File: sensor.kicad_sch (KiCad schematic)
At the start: 35 parts, among them J10 Conn_01x01_Pin, J5 Conn_01x07_Pin, J8 Conn_01x08_Pin, U4 mXT336UD-MAU002, U5 MIC5504-3.3YM5

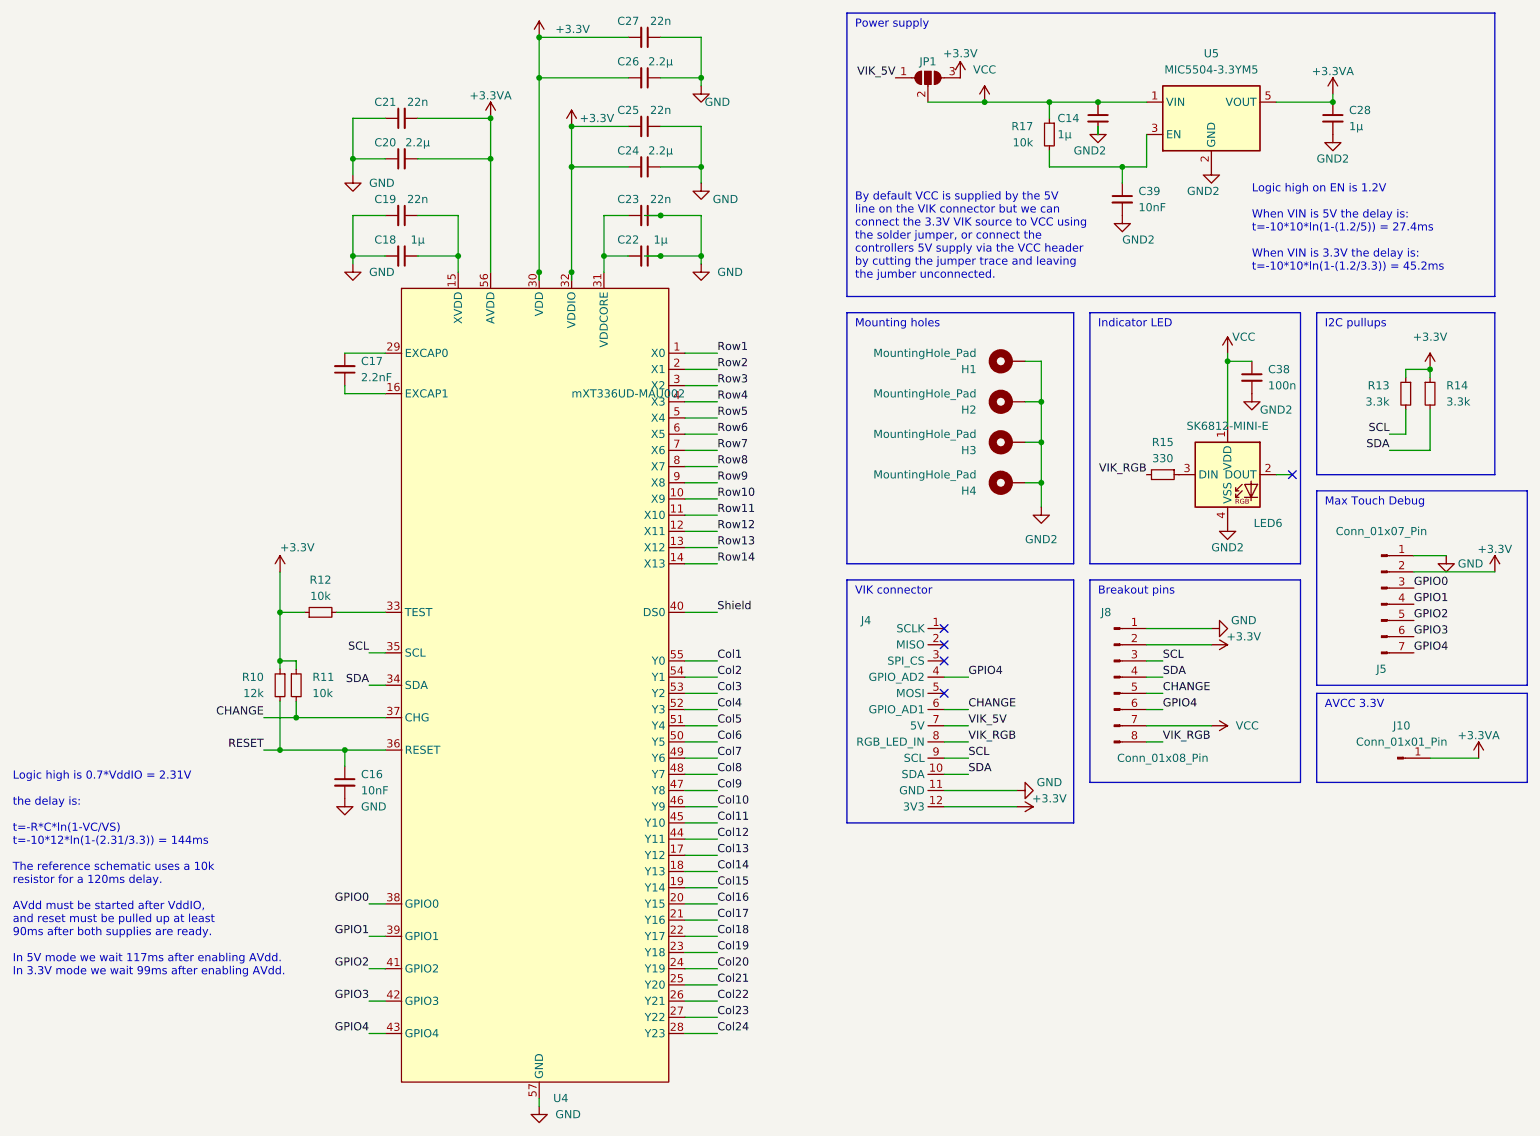
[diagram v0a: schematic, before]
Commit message: smashed everything into one PCB and removed some parts I don't want.
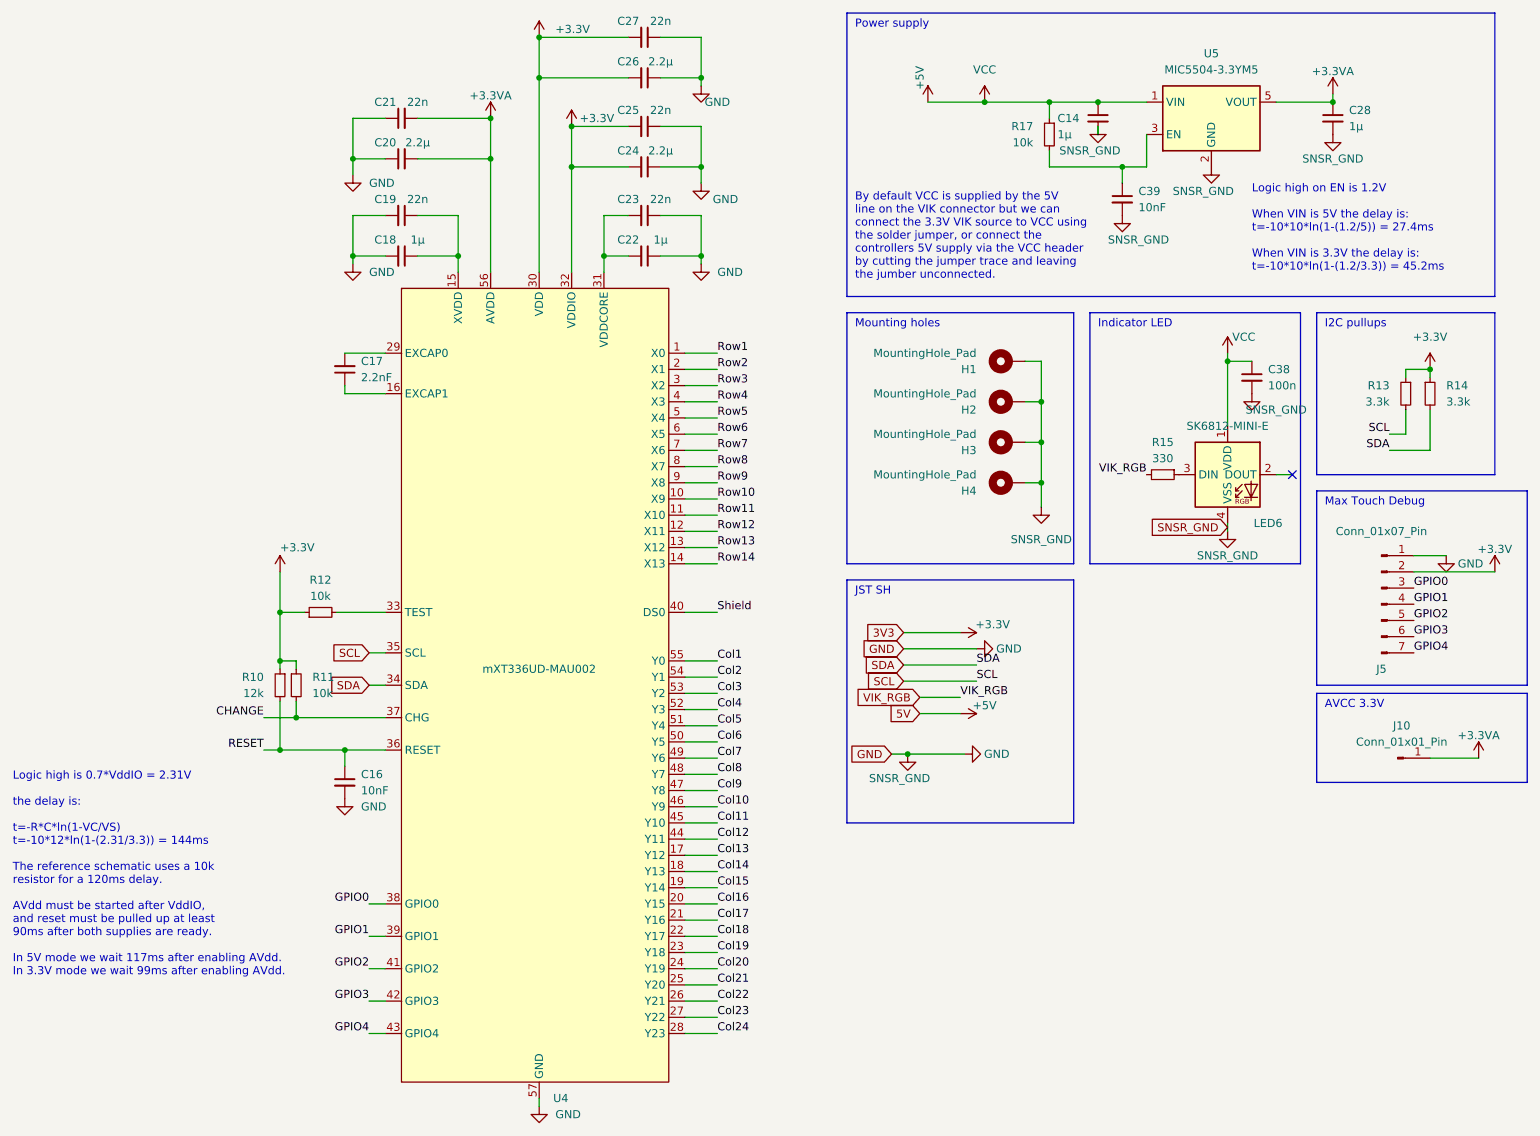
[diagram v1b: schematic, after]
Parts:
- removed J4: ~, Vik:vik-module-connector-vertical, symbol Vik:vik-module-connector
- removed J8: Conn_01x08_Pin, Connector_PinHeader_2.54mm:PinHeader_1x08_P2.54mm_Vertical, symbol Connector:Conn_01x08_Pin
- removed JP1: SolderJumper_3_Open, Jumper:SolderJumper-3_P1.3mm_Bridged2Bar12_RoundedPad1.0x1.5mm, symbol Jumper:SolderJumper_3_Open
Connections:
- net GND2 renamed GND
- net VCC renamed +5V
- no-connect marks 5 -> 1
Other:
- note added: "JST SH"
- note removed: "Breakout pins"
- note removed: "VIK connector"
